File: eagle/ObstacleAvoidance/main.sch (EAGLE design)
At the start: 14 parts, among them IC2 L293D, X1 JST-XH-02-PIN-LONG-PAD, X2 JST-XH-02-PIN-LONG-PAD, X3 JST-XH-04-PIN-LONG-PAD

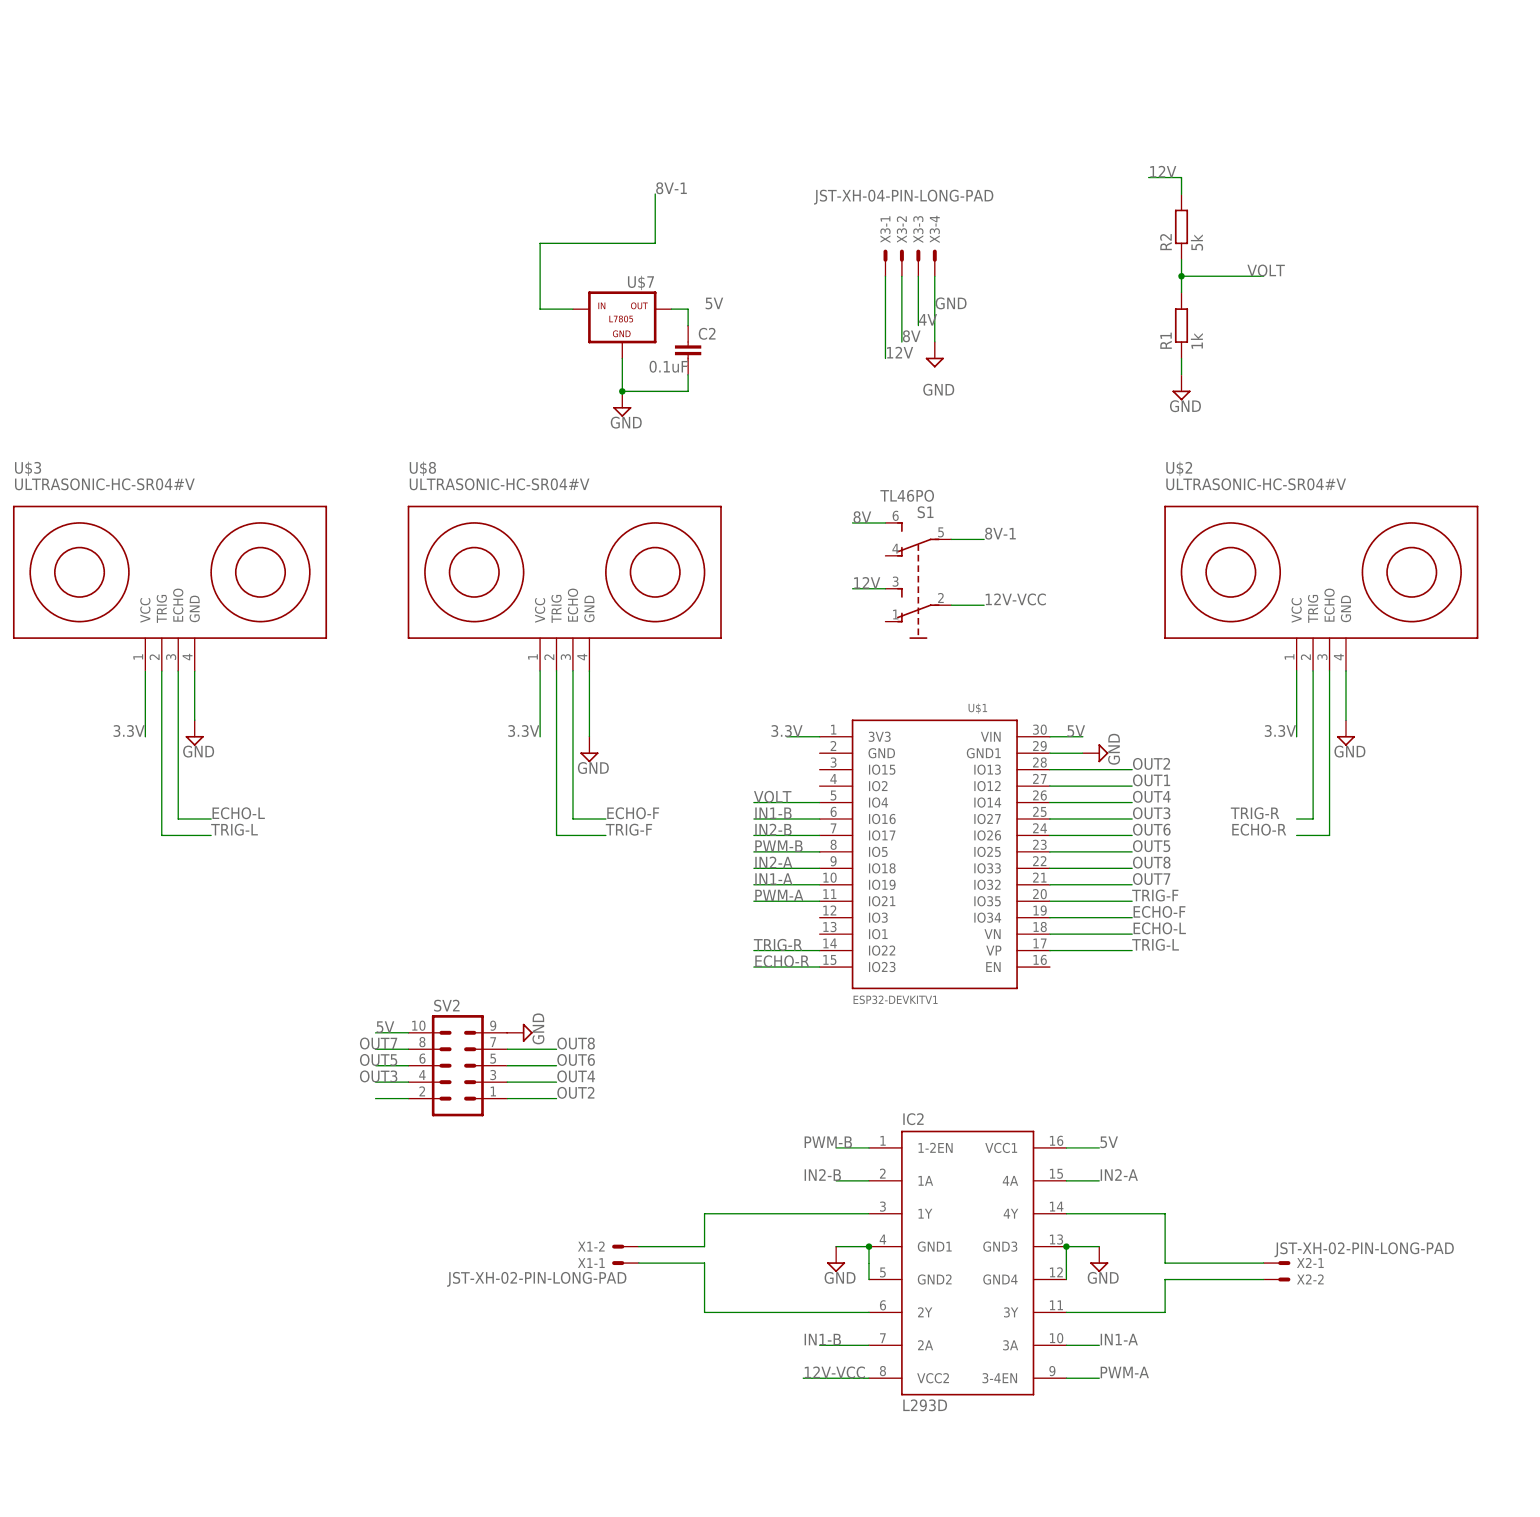
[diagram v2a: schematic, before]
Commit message: Feat: PCB printing files
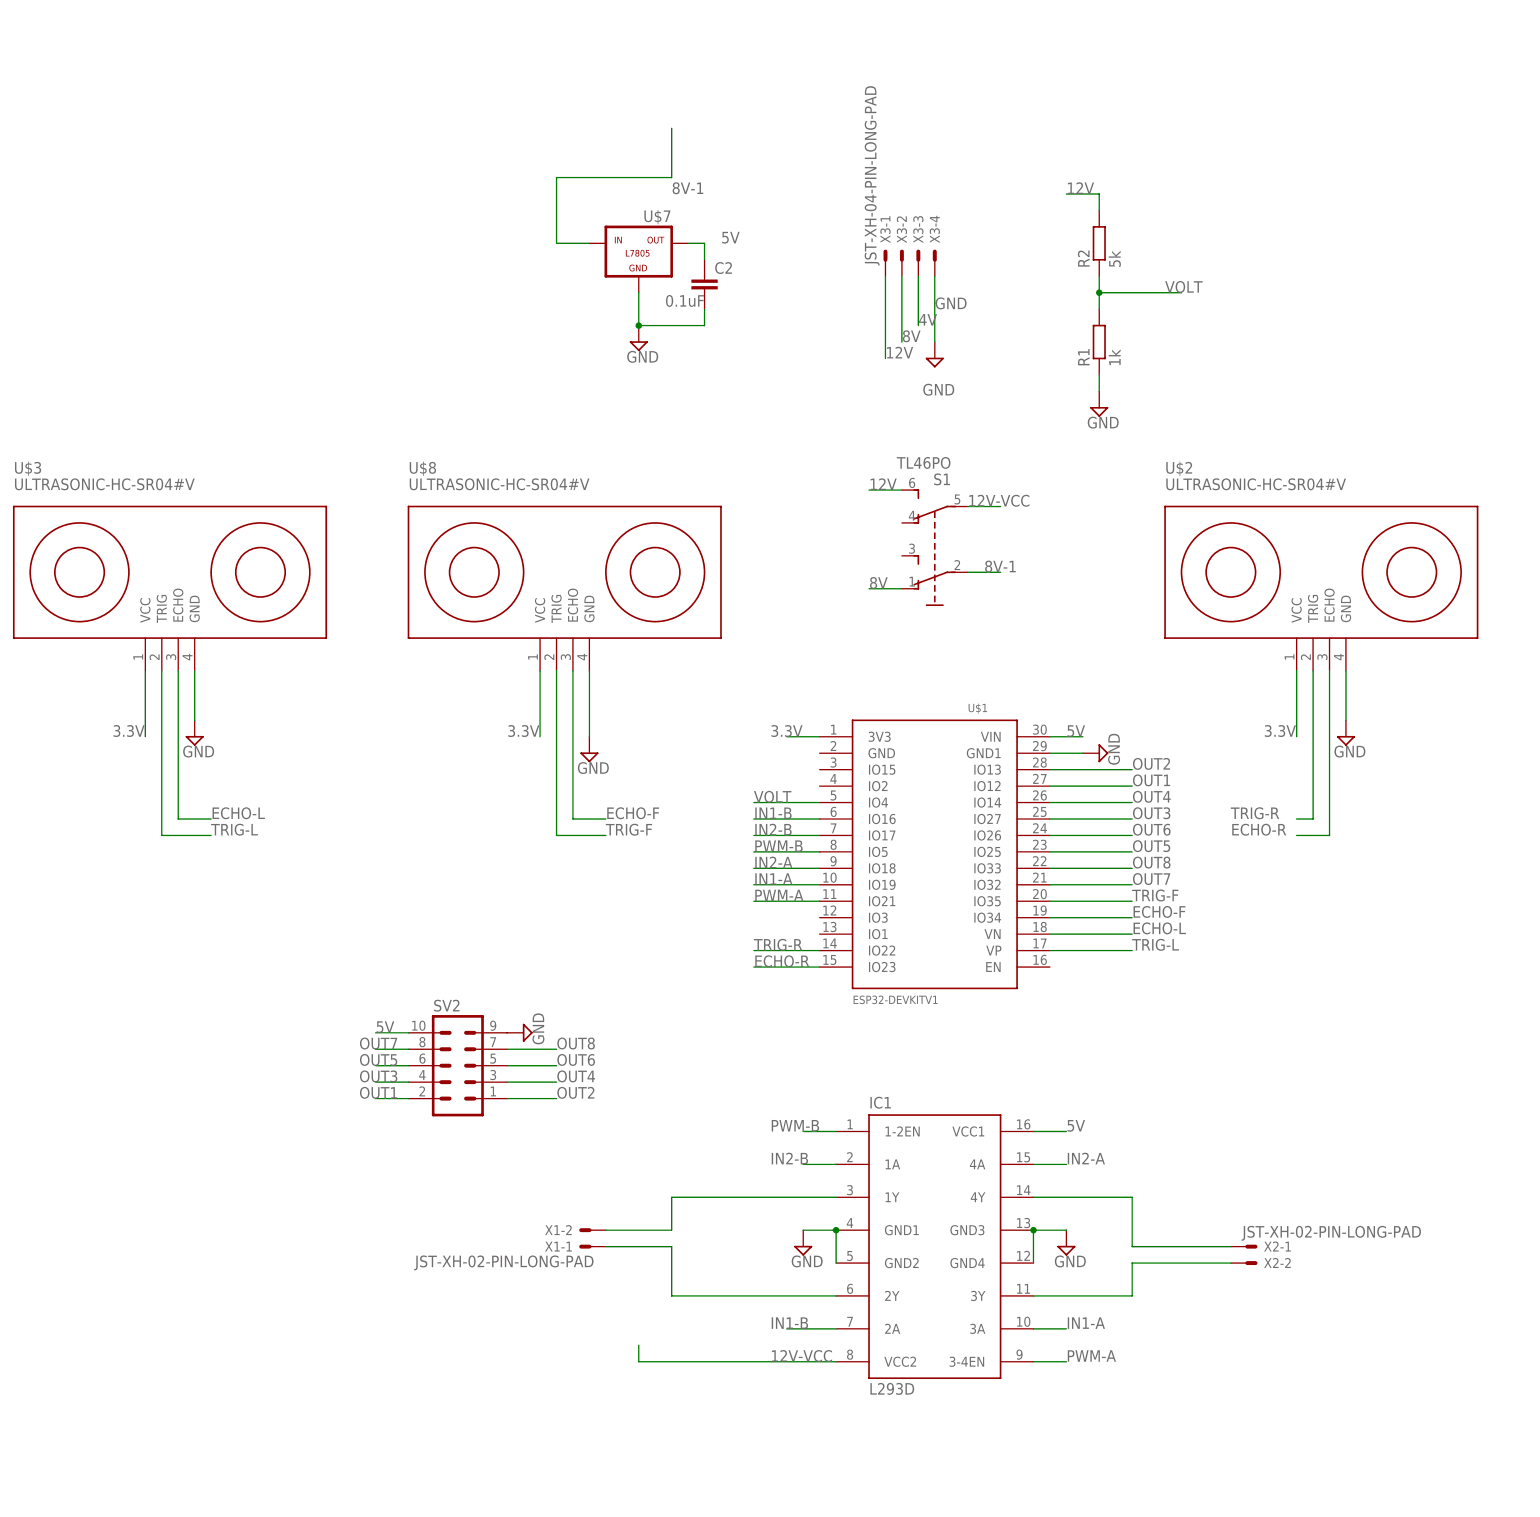
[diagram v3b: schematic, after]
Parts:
- removed IC2: L293D, st-microelectronics:L293D
- added IC1: L293D, st-microelectronics:L293D
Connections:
- removed net N$5: IC2.GND2
- removed net N$6: IC2.GND4
- removed net OUT9: SV2.2
- net 12V: now also S1.S1; no longer S1.S
- net 12V-VCC: now also IC1.VCC2, S1.P1; no longer IC2.VCC2, S1.P
- net 5V: now also IC1.VCC1; no longer IC2.VCC1
- net 8V: now also S1.O; no longer S1.S1
- net 8V-1: now also S1.P; no longer S1.P1
- net GND: now also IC1.GND1, IC1.GND2, IC1.GND3, IC1.GND4; no longer IC2.GND1, IC2.GND3
- net IN1-A: now also IC1.3A; no longer IC2.3A
- net IN1-B: now also IC1.2A; no longer IC2.2A
- net IN2-A: now also IC1.4A; no longer IC2.4A
- net IN2-B: now also IC1.1A; no longer IC2.1A
- net N$1: now also IC1.1Y; no longer IC2.1Y
- net N$2: now also IC1.2Y; no longer IC2.2Y
- net N$3: now also IC1.4Y; no longer IC2.4Y
- net N$4: now also IC1.3Y; no longer IC2.3Y
- net OUT1: now also SV2.2
- net PWM-A: now also IC1.3-4EN; no longer IC2.3-4EN
- net PWM-B: now also IC1.1-2EN; no longer IC2.1-2EN
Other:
- moved on the sheet: C2, R1, R2, S1, U$7, X1-1, X1-2, X2-1, X2-2
